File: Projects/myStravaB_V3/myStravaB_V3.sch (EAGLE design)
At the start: 68 parts, among them IC1 TPS63051RMWT, IC2 BMD-340-A-R, IC3 BME280, J1 47571-0001, Q2 BSS138BKW, U1 FXOS8700CQR1, U2 MCP73831, U3 FM24CL16B, Y3 32.768kHz

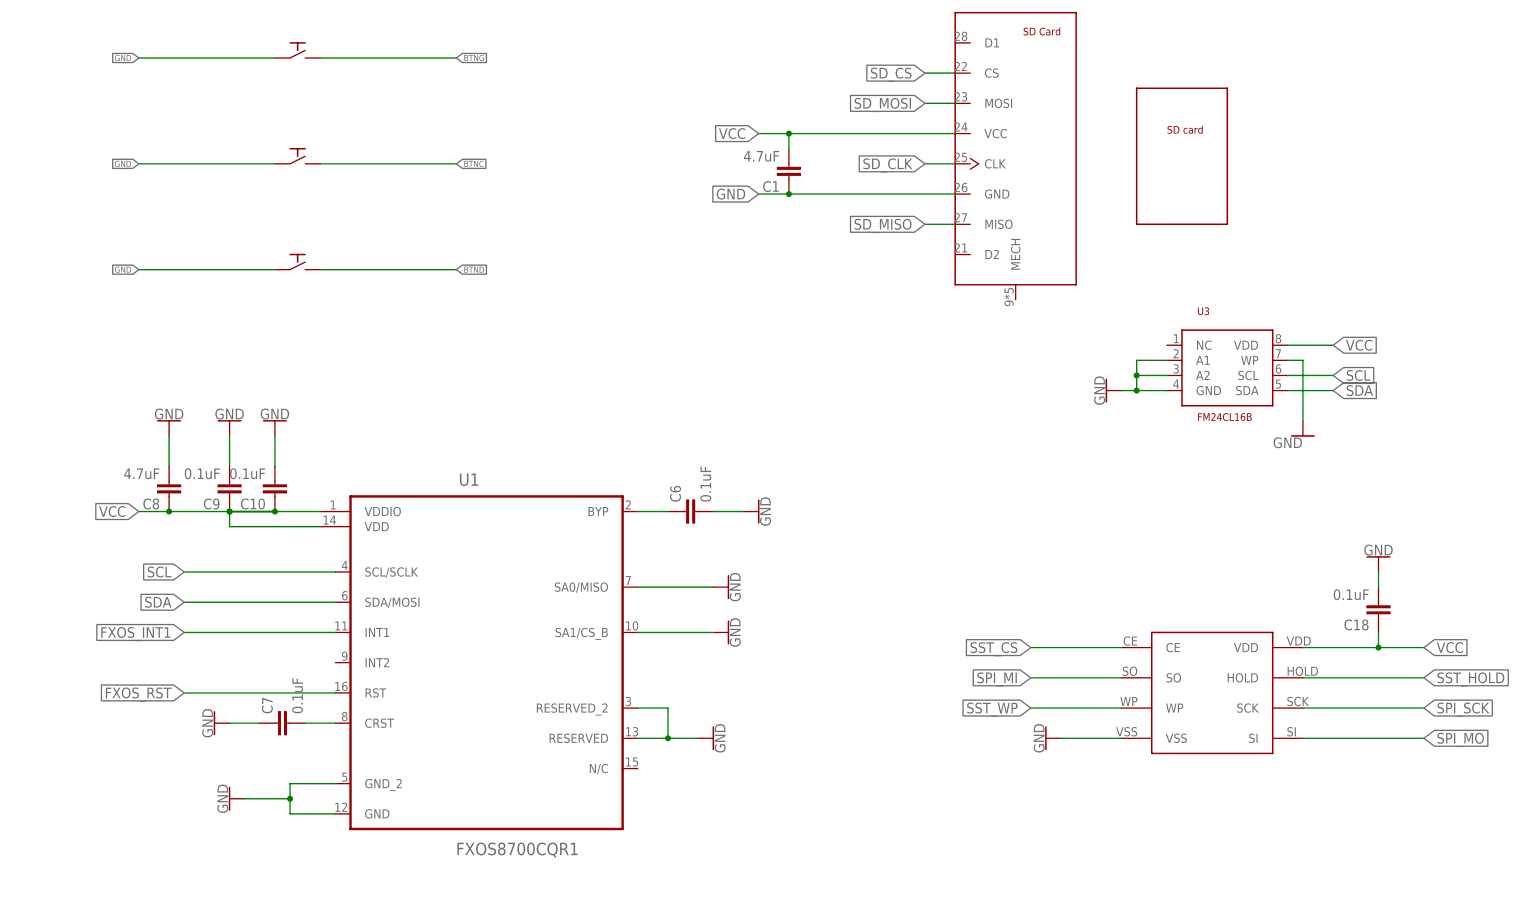
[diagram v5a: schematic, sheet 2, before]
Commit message: Updated 5V boost DCDC converter
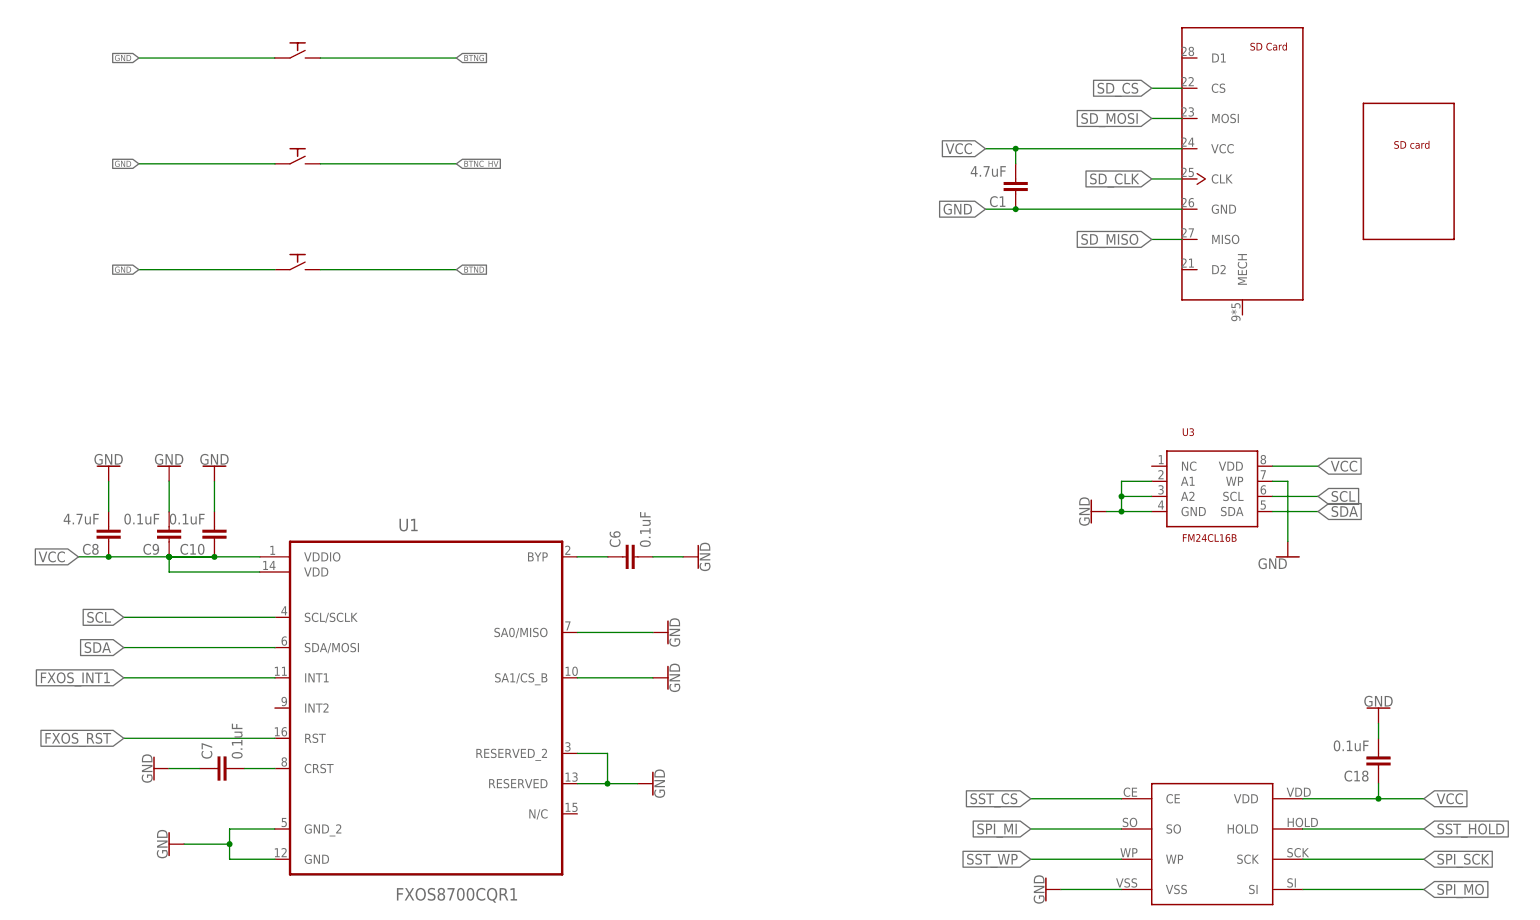
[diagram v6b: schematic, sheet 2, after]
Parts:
- added C2, C3: 10uF, rcl:C-EUC0805
- added C4: 220nF, rcl:C-EUC0805
- added D1: BAT54C, diode:BAT54C
- U4: value (none) -> REG710; device PowerSupplies:TPS7A05XX -> DCDC:REG710
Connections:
- new net BTNC_HV: D1.CC, SPST2.P$2
- new net N$5: C4.1, U4.PUMP+
- new net N$6: C4.2, U4.PUMP-
- net 5V: now also C3.2, U4.VOUT; no longer U4.OUT
- net BTNC: now also D1.A1; no longer SPST2.P$2
- net GND: now also C2.1, C3.1
- net SWON: now also D1.A2
- net VIN: now also C2.2, U4.VIN; no longer U4.IN
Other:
- moved on the sheet: C1, C10, C18, C6, C7, C8, C9, M2, R3, U1, U3

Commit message: Updated stravaV3 Updated Climber
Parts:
- IC1: device SamacSys_Parts:TPS63051RMWT -> DCDC:TPS63051RMWT
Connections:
- net SCL: now also J1.MOSI
- net SDA: now also J1.CS
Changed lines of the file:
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@@
 <drawing>
 <settings>
-<setting alwaysvectorfont="yes"/>
+<setting alwaysvectorfont="no"/>
 <setting keepoldvectorfont="yes"/>
 <setting verticaltext="up"/>
@@
 <part name="R19" library="SparkFun-Resistors" deviceset="4.7KOHM" device="-0603-1/10W-1%" value="10k"/>
 <part name="GND74" library="SparkFun-PowerSymbols" deviceset="GND" device=""/>
-<part name="IC1" library="SamacSys_Parts" deviceset="TPS63051RMWT" device=""/>
+<part name="IC1" library="DCDC" deviceset="TPS63051RMWT" device=""/>
 <part name="GND10" library="SparkFun-PowerSymbols" deviceset="GND" device=""/>
 <part name="C11" library="rcl" library_urn="urn:adsk.eagle:library:334" deviceset="C-EU" device="C0805" package3d_urn="urn:adsk.eagle:package:23617/2" value="10uF"/>
@@
 <label x="-22.86" y="281.94" size="1.27" layer="95" xref="yes"/>
 </segment>
+<segment>
+<pinref part="J1" gate="G$1" pin="MOSI"/>
+<wire x1="76.2" y1="284.48" x2="66.04" y2="284.48" width="0.1524" layer="91"/>
+<label x="66.04" y="284.48" size="1.016" layer="95" rot="R180" xref="yes"/>
+</segment>
 </net>
 <net name="SDA" class="0">
@@
 <label x="-22.86" y="284.48" size="1.27" layer="95" xref="yes"/>
 </segment>
+<segment>
+<pinref part="J1" gate="G$1" pin="CS"/>
+<wire x1="76.2" y1="289.56" x2="66.04" y2="289.56" width="0.1524" layer="91"/>
+<label x="66.04" y="289.56" size="1.016" layer="95" rot="R180" xref="yes"/>
+</segment>
 </net>

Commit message: Order @ Boktech
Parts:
- R14, R18, R19: value 10k -> 47k
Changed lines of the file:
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@@
 <drawing>
 <settings>
-<setting alwaysvectorfont="no"/>
+<setting alwaysvectorfont="yes"/>
 <setting keepoldvectorfont="yes"/>
 <setting verticaltext="up"/>
@@
 <part name="L4" library="adafruit" deviceset="WS2812B" device=""/>
 <part name="Q2" library="BSS138" deviceset="BSS138BKW" device=""/>
-<part name="R18" library="SparkFun-Resistors" deviceset="4.7KOHM" device="-0603-1/10W-1%" value="10k"/>
-<part name="R19" library="SparkFun-Resistors" deviceset="4.7KOHM" device="-0603-1/10W-1%" value="10k"/>
+<part name="R18" library="SparkFun-Resistors" deviceset="4.7KOHM" device="-0603-1/10W-1%" value="47k"/>
+<part name="R19" library="SparkFun-Resistors" deviceset="4.7KOHM" device="-0603-1/10W-1%" value="47k"/>
 <part name="GND74" library="SparkFun-PowerSymbols" deviceset="GND" device=""/>
 <part name="IC1" library="DCDC" deviceset="TPS63051RMWT" device=""/>
@@
 <part name="R12" library="rcl" library_urn="urn:adsk.eagle:library:334" deviceset="R-US_" device="R0603" package3d_urn="urn:adsk.eagle:package:23555/3" value="100k"/>
 <part name="L1" library="SamacSys_Parts" deviceset="1269AS-H-1R5M=P2" device=""/>
-<part name="R14" library="rcl" library_urn="urn:adsk.eagle:library:334" deviceset="R-US_" device="R0603" package3d_urn="urn:adsk.eagle:package:23555/3" value="10k"/>
+<part name="R14" library="rcl" library_urn="urn:adsk.eagle:library:334" deviceset="R-US_" device="R0603" package3d_urn="urn:adsk.eagle:package:23555/3" value="47k"/>
 <part name="GND14" library="SparkFun-PowerSymbols" deviceset="GND" device=""/>
 <part name="U$6" library="STC3100" deviceset="STC3100" device=""/>
@@
 <attribute name="VALUE" x="71.12" y="-7.62" size="1.778" layer="94" font="vector"/>
 </instance>
-<instance part="C2" gate="G$1" x="40.64" y="-5.08" smashed="yes" rot="R180">
+<instance part="C2" gate="G$1" x="40.64" y="-5.08" smashed="yes" rot="R180" grouprefs="POWER">
 <attribute name="NAME" x="39.116" y="-5.461" size="1.778" layer="95" rot="R180"/>
 <attribute name="VALUE" x="39.116" y="-0.381" size="1.778" layer="96" rot="R180"/>
 </instance>
-<instance part="C3" gate="G$1" x="114.3" y="-5.08" smashed="yes" rot="R180">
+<instance part="C3" gate="G$1" x="114.3" y="-5.08" smashed="yes" rot="R180" grouprefs="POWER">
 <attribute name="NAME" x="112.776" y="-5.461" size="1.778" layer="95" rot="R180"/>
 <attribute name="VALUE" x="112.776" y="-0.381" size="1.778" layer="96" rot="R180"/>
 </instance>
-<instance part="C4" gate="G$1" x="83.82" y="15.24" smashed="yes" rot="R270">
+<instance part="C4" gate="G$1" x="83.82" y="15.24" smashed="yes" rot="R270" grouprefs="POWER">
 <attribute name="NAME" x="84.201" y="13.716" size="1.778" layer="95" rot="R270"/>
 <attribute name="VALUE" x="79.121" y="13.716" size="1.778" layer="96" rot="R270"/>
